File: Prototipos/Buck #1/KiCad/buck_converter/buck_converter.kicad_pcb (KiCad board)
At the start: 2 copper layers, 32 parts, among them J1 Conn_01x03_Pin, J2 Screw_Terminal_01x02, J3 Screw_Terminal_01x02, Q1 IRF9540NPBF, Q2 IRLML6344, Q3 NPN

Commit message: Avances en PCB convertidor buck
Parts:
- added J4: Conn_01x03_Pin, Connector_PinHeader_2.54mm:PinHeader_1x03_P2.54mm_Vertical, F.Cu at (99.1, 88.9)
- added J5: Conn_01x03_Pin, Connector_PinHeader_2.54mm:PinHeader_1x03_P2.54mm_Vertical, F.Cu at (99.1, 81.3)
- added J6: Conn_01x03_Pin, Connector_PinHeader_2.54mm:PinHeader_1x03_P2.54mm_Vertical, F.Cu at (99.1, 76.2)
- J2, J3: footprint TerminalBlock_TE-Connectivity:TerminalBlock_TE_282834-2_1x02_P2.54mm_Horizontal -> TerminalBlock_Phoenix:TerminalBlock_Phoenix_MKDS-1,5-2-5.08_1x02_P5.08mm_Horizontal
- moved C6 17.8 mm to (132.1, 91.4)
- moved C1 17.8 mm to (127.0, 91.4), turned to 180 degrees
- moved J3 13.7 mm to (132.1, 66.0)
- moved R10 12.7 mm to (132.1, 81.3)
- moved C3 12.7 mm to (121.9, 83.8)
- moved C5 12.7 mm to (127.0, 76.2)
- moved D4 12.7 mm to (114.3, 76.2)
- moved R14 12.7 mm to (116.9, 76.2)
- moved R5 12.7 mm to (121.9, 73.7)
- moved R7 12.7 mm to (127.0, 78.7)
- moved R8 12.7 mm to (129.3, 86.4)
- moved R9 12.7 mm to (134.6, 78.7)
- moved C7 12.7 mm to (116.9, 86.4)
- moved D2 12.7 mm to (119.4, 73.7)
- moved Q3 12.7 mm to (107.9, 78.8)
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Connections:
- D1 pad 1: Net-(D1-K) -> 12V
- D3 pad 1: Gate -> Gate_MOSFET
- D4 pad 1: Gate -> Gate_BJT
- J2 pad 1: Net-(D1-K) -> 12V
- Q1 pad 3: Net-(D1-K) -> 12V
- Q2 pad 3: Gate -> Gate_MOSFET
- Q3 pad 1: Gate -> Gate_BJT
- R1 pad 1: PWM_micro -> PWM_MOSFET
- R11 pad 1: PWM_micro -> PWM_BJT
- R12 pad 1: 12V -> 12V_BJT
- R12 pad 2: Gate -> Gate_BJT
- R14 pad 1: Gate -> Gate_BJT
- R2 pad 1: Net-(D1-K) -> 12V
- R3 pad 1: 12V -> 12V_MOSFET
- R3 pad 2: Gate -> Gate_MOSFET
- R6 pad 1: Gate -> Gate_MOSFET
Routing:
- net PGND: track 161.3 -> 193.9 mm, vias 0 -> 1
- net Gate_MOSFET: track 0.00 -> 25.7 mm, vias 0 -> 11
- net Gate_BJT: track 0.00 -> 25.4 mm, vias 0 -> 11
- net 12V: track 5.08 -> 30.5 mm, vias 0 -> 13
- net Gate: track 53.4 -> 33.0 mm, vias 0 -> 14
- net Net-(D1-K): track 12.7 -> 0.00 mm
- net Net-(D1-A): track 30.6 -> 43.2 mm, vias 0 -> 18
- net PWM_BJT: track 0.00 -> 7.81 mm, vias 0 -> 4
- net Net-(Q2-Pad1): track 19.5 -> 27.1 mm
- net AGND: track 2.56 -> 7.66 mm, vias 0 -> 4
- net Retro_micro: track 17.8 -> 22.9 mm, vias 0 -> 10
- net PWM_MOSFET: track 0.00 -> 2.54 mm, vias 0 -> 2
- net Net-(Q3-B): track 15.3 -> 12.7 mm, vias 0 -> 6
- net 12V_MOSFET: track 0.00 -> 2.54 mm, vias 0 -> 2
- net 12V_BJT: track 0.00 -> 2.54 mm, vias 0 -> 2
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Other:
- board outline added: 73.7 x 38.1 mm
- board text added: "1"
- board text added: "10"
- board text added: "11"
- board text added: "12"
- board text added: "13"
- board text added: "2"
- board text added: "3"
- board text added: "4"
- board text added: "5"
- board text added: "6"
- board text added: "7"
- board text added: "8"
- board text added: "9"
- board text added: "A"
- board text added: "B"
- board text added: "C"
- board text added: "D"
- board text added: "E"
- board text added: "F"
- board text added: "G"
- board text added: "H"
- board text added: "I"
- board text added: "J"
- board text added: "K"
- board text added: "L"
- board text added: "M"
- board text added: "N"
- board text added: "O"
- board text added: "P"
- board text added: "Q"
- board text added: "R"
- board text added: "S"
- board text added: "T"
- board text added: "V"
- board text added: "W"
- board text added: "X"
- board text added: "Y"
- board text added: "Z"

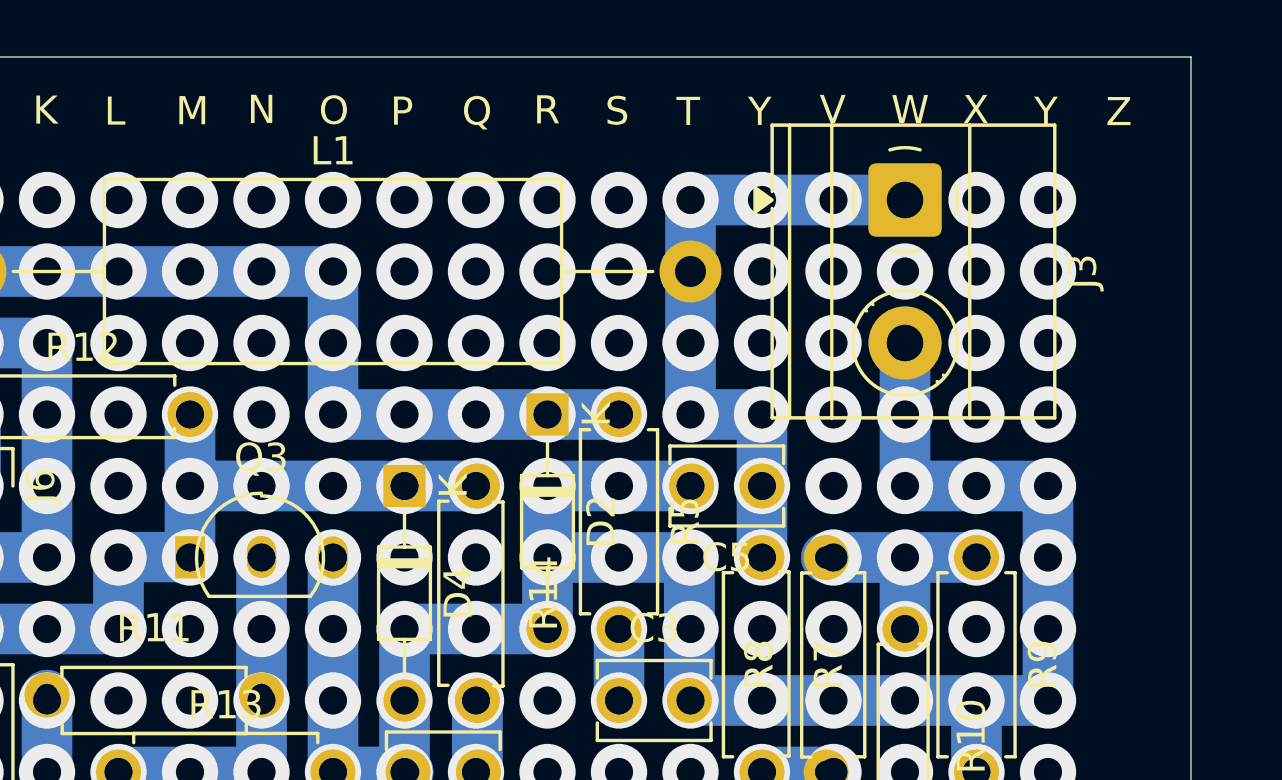
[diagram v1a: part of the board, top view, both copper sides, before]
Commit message: Corrección footprint transistor
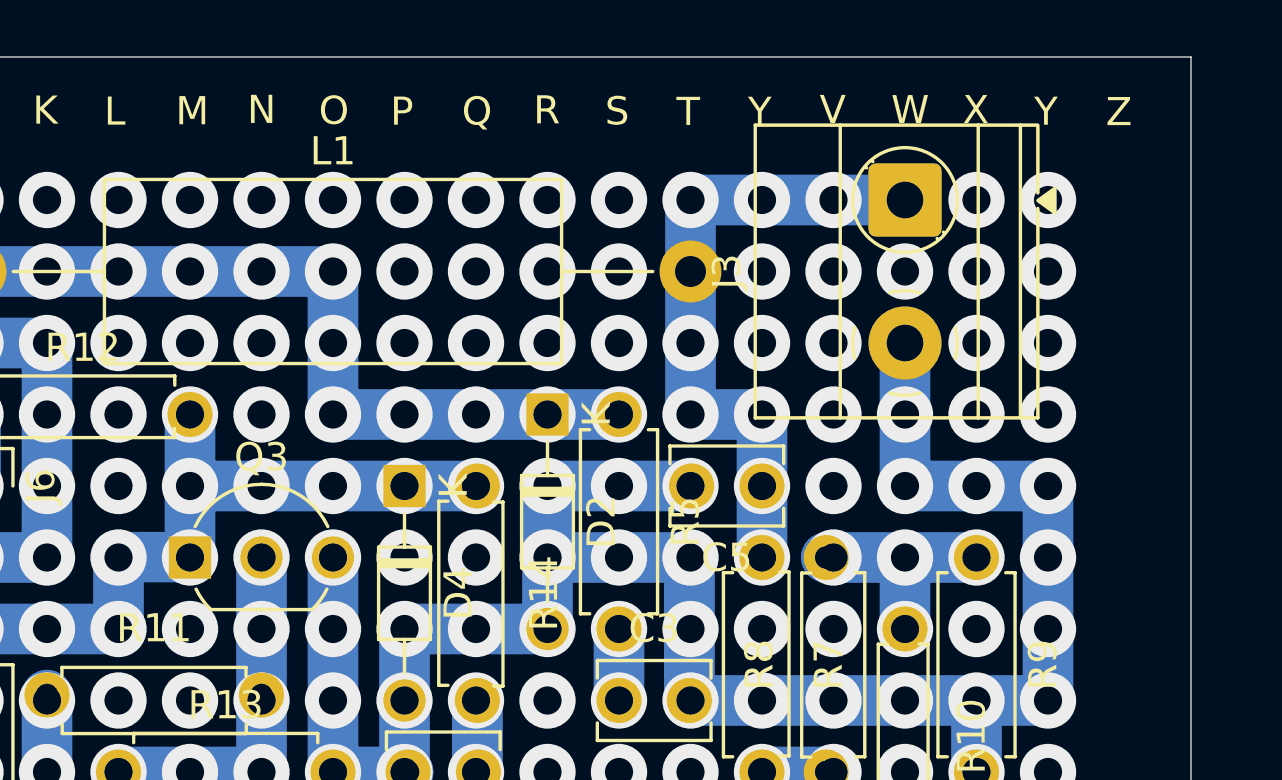
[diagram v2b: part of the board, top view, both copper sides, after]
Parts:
- C7: value ~ -> 2p
- Q3: footprint Package_TO_SOT_THT:TO-92_Inline -> Package_TO_SOT_THT:TO-92_Inline_Wide
- R11: value ~ -> 33k
- R12: value ~ -> 120
- R14: value ~ -> 180
- moved J3 5.08 mm to (132.1, 71.1), turned to 90 degrees
- moved Q3 1.27 mm to (106.7, 78.7)

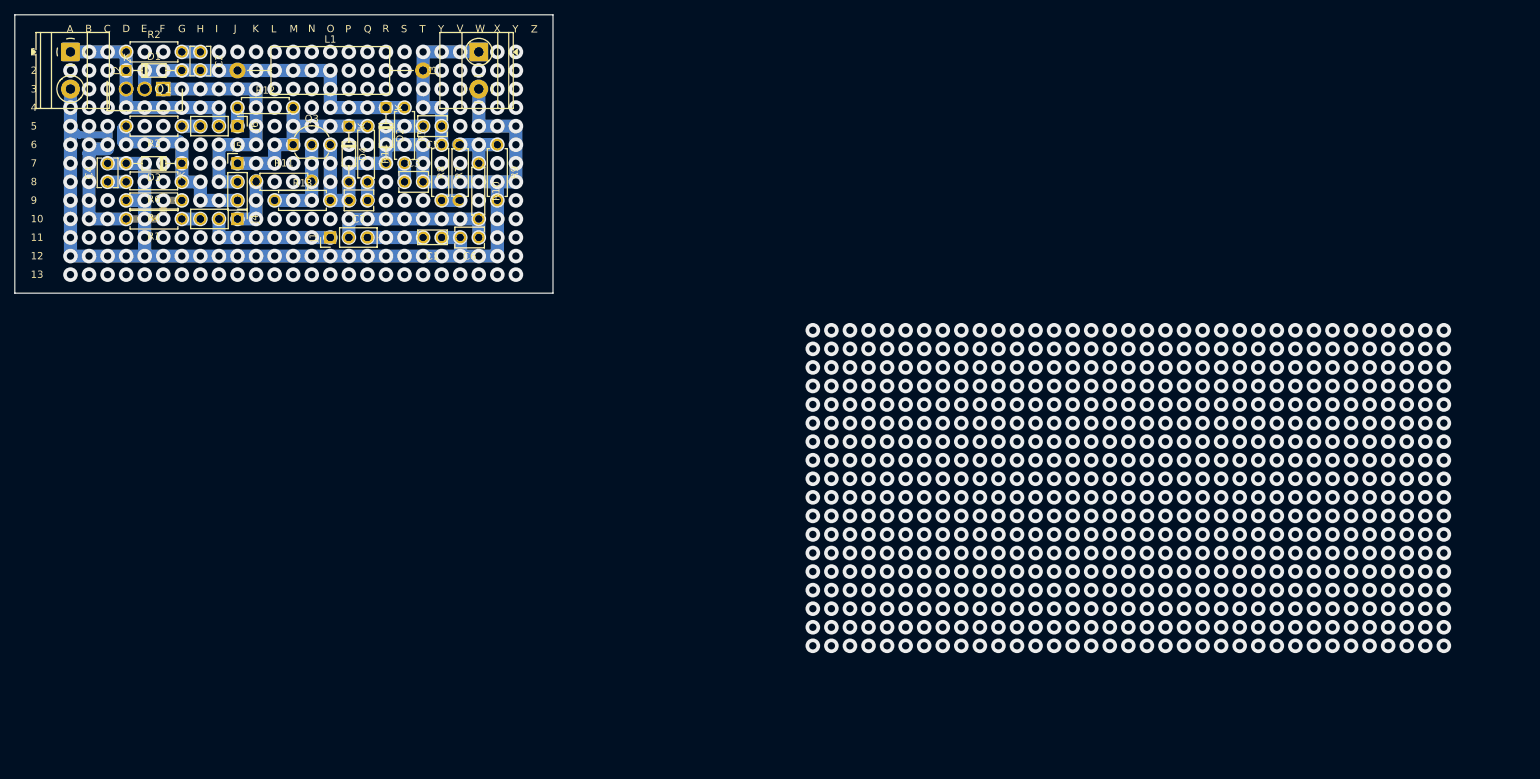
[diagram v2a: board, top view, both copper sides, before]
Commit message: Corrección PCB Buck, para disminuir tamaño
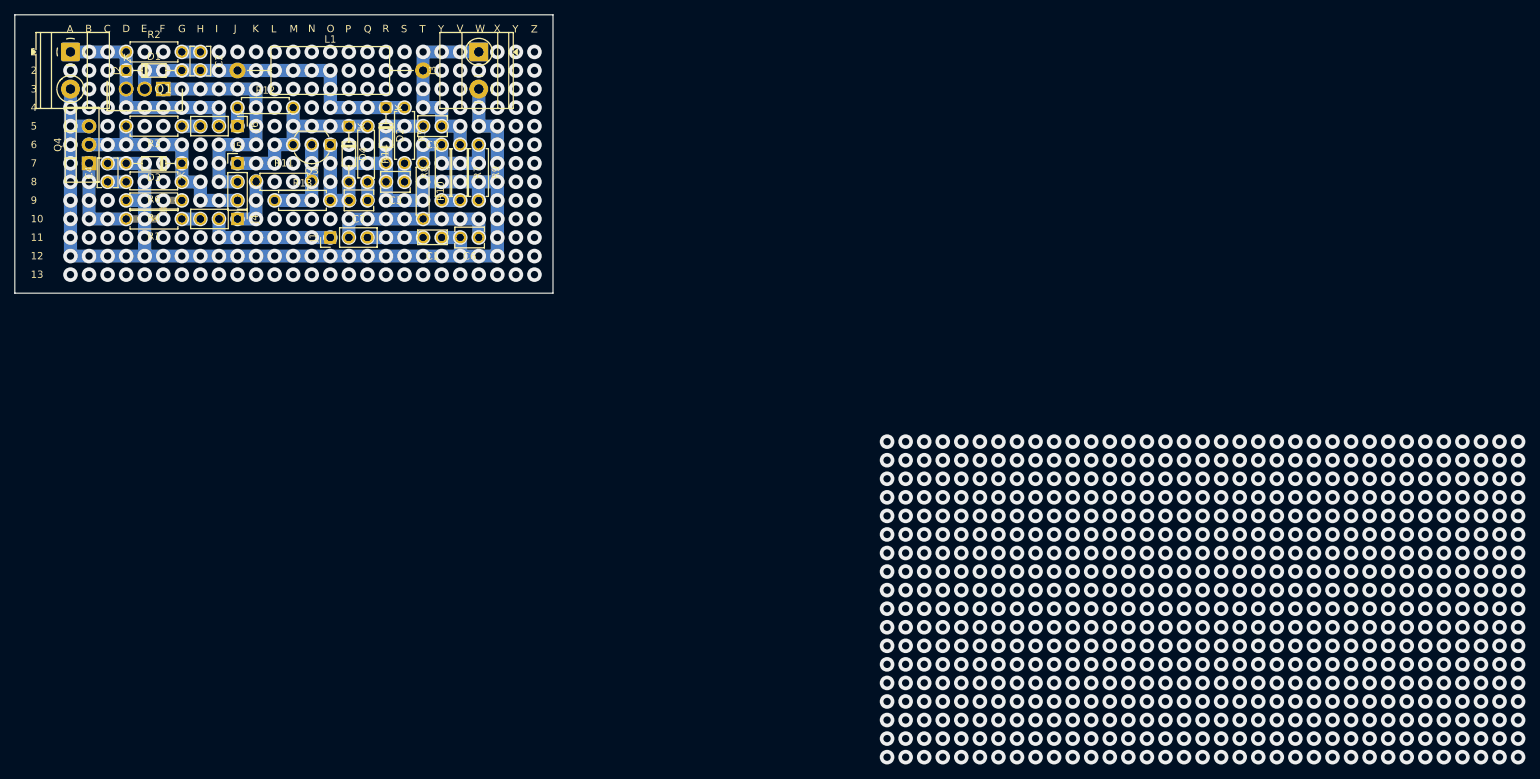
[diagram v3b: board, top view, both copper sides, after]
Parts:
- removed Q2: IRLML6344, KICAD-Libraries:SOT23
- added Q4: NMOS, Package_TO_SOT_THT:TO-220-3_Vertical, F.Cu at (78.7, 81.3)
- moved R10 7.62 mm to (124.5, 81.3)
- moved Q3 5.08 mm to (111.8, 78.7), turned to 180 degrees
- moved R9 2.59 mm to (132.0, 78.7)
- moved R7 2.54 mm to (129.5, 78.7)
- moved R8 2.28 mm to (127.0, 86.4)
- turned C3 to 180 degrees
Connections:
- Q3 pad 1: Gate_BJT -> PGND
- Q3 pad 3: PGND -> Gate_BJT
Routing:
- net Net-(R10-Pad1): track 7.88 -> 15.3 mm, vias 4 -> 7
- net Gate_MOSFET: track 25.7 -> 30.5 mm, vias 11 -> 13
- net Net-(Q4-G): track 27.1 -> 22.9 mm
- net PGND: track 193.9 -> 190.9 mm, vias 1 -> 0
- net Net-(J3-Pin_1): track 22.9 -> 25.4 mm, vias 10 -> 11
- net (no net): vias 825 -> 833

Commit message: Modificaciones varias para facilitar visualización
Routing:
- net PGND: vias 0 -> 76
- net Net-(Q4-G): vias 0 -> 7
- net (no net): vias 833 -> 120
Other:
- board size 73.7 x 38.1 mm -> 72.7 x 38.1 mm
